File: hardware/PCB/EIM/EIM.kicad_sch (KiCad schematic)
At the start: 37 parts, among them U1 AD9834BRUZ, U2 AD8130ARZ, U3 AD8014ARZ-REEL

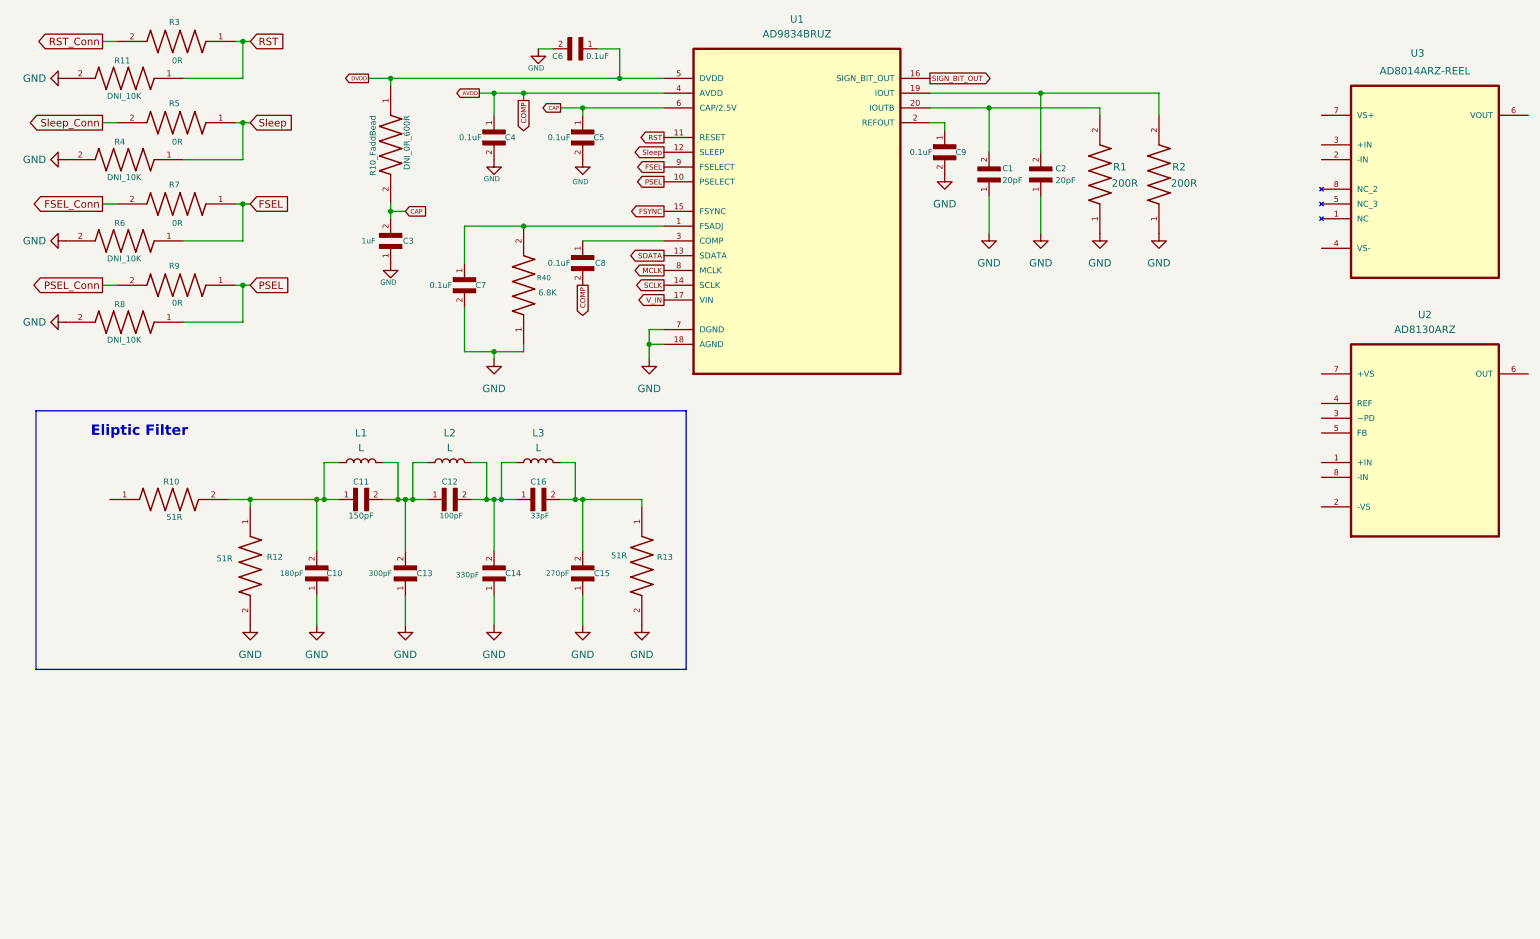
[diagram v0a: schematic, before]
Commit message: MAMS-33 Update schematic for AD9834 and AD8130
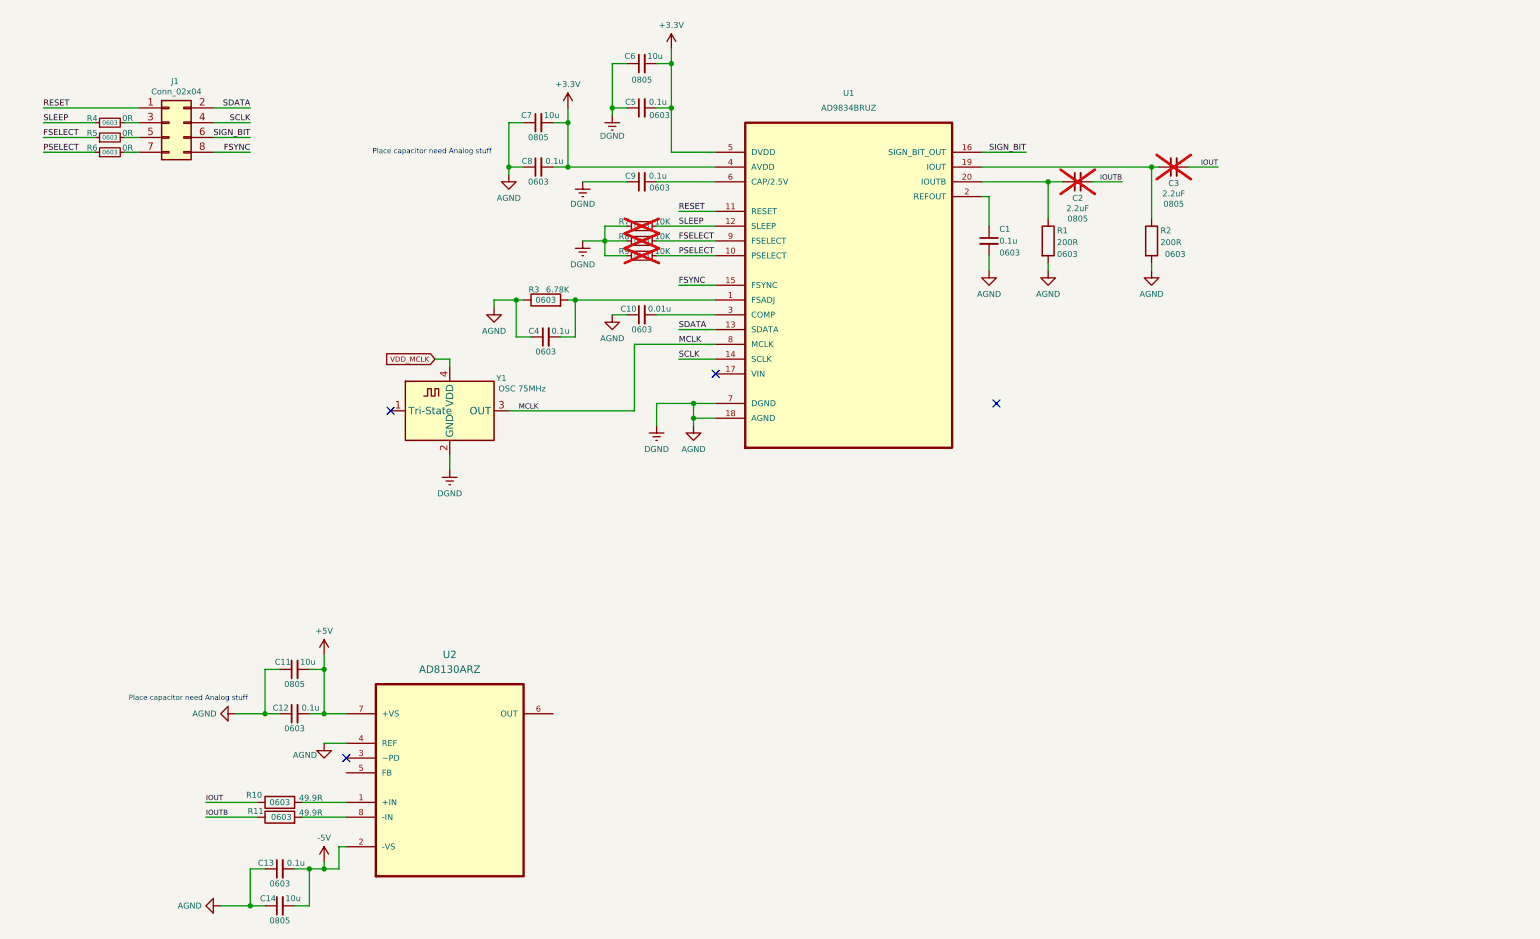
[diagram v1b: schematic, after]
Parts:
- removed C1, C2: 20pF, VJ0603D240KXCAP:CAPC1608X94N, symbol Capacitor_0603:VJ0603D240KXCAP
- removed C10: 180pF, VJ0603D240KXCAP:CAPC1608X94N, symbol Capacitor_0603:VJ0603D240KXCAP
- removed C11: 150pF, VJ0402D3R3DXCAP:CAPC1005X61N, symbol VJ0402D3R3DXCAP:VJ0402D3R3DXCAP
- removed C12: 100pF, VJ0603D240KXCAP:CAPC1608X94N, symbol Capacitor_0603:VJ0603D240KXCAP
- removed C13: 300pF, VJ0603D240KXCAP:CAPC1608X94N, symbol Capacitor_0603:VJ0603D240KXCAP
- removed C14: 330pF, VJ0603D240KXCAP:CAPC1608X94N, symbol Capacitor_0603:VJ0603D240KXCAP
- removed C15: 270pF, VJ0603D240KXCAP:CAPC1608X94N, symbol Capacitor_0603:VJ0603D240KXCAP
- removed C16: 33pF, VJ0603D240KXCAP:CAPC1608X94N, symbol Capacitor_0603:VJ0603D240KXCAP
- removed C3: 1uF, VJ0603D240KXCAP:CAPC1608X94N, symbol Capacitor_0603:VJ0603D240KXCAP
- removed C4, C5, C6, C7, C8, C9: 0.1uF, VJ0402D3R3DXCAP:CAPC1005X61N, symbol VJ0402D3R3DXCAP:VJ0402D3R3DXCAP
- removed L1, L2, L3: L, symbol Device:L
- removed R1, R2: 200R, ERA3AED203V:RES_ERA3AED203V, symbol Resistor_0603:ERA3AED203V
- removed R10, R12, R13: 51R, ERA3AED203V:RES_ERA3AED203V, symbol Resistor_0603:ERA3AED203V
- removed R10_FaddBead: DNI_0R_600R, ERA3AED203V:RES_ERA3AED203V, symbol Resistor_0603:ERA3AED203V
- removed R11, R4, R6, R8: DNI_10K, ERA3AED203V:RES_ERA3AED203V, symbol Resistor_0603:ERA3AED203V
- removed R3, R5, R7, R9: 0R, ERA3AED203V:RES_ERA3AED203V, symbol Resistor_0603:ERA3AED203V
- removed R40: 6.8K, ERA3AED203V:RES_ERA3AED203V, symbol Resistor_0603:ERA3AED203V
- removed U3: AD8014ARZ-REEL, AD8014ARZ-REEL:SOIC127P600X175-8N, symbol AD8014ARZ-REEL:AD8014ARZ-REEL
- added C1, C12, C13, C4, C5, C8, C9: 0.1u, 0603, symbol Device:C_Small
- added C10: 0.01u, 0603, symbol Device:C_Small
- added C11, C14, C6, C7: 10u, 0805, symbol Device:C_Small
- added C2, C3: 2.2uF, 0805, symbol Device:C_Small
- added J1: Conn_02x04, Connector_PinHeader_2.54mm:PinHeader_2x04_P2.54mm_Vertical, symbol Connector_Generic:Conn_02x04_Odd_Even
- added R1, R2: 200R, 0603, symbol Device:R
- added R10, R11: 49.9R, 0603, symbol Device:R
- added R3: 6.78K, 0603, symbol Device:R
- added R4, R5, R6: 0R, 0603, symbol Device:R_Small
- added R7, R8, R9: 10K, 0603, symbol Device:R_Small
- added Y1: OSC 75MHz, Oscillator_SMD_2.5x2.0mm, symbol Oscillator:ECS-2520MV-xxx-xx
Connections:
- net DVDD is gone; now on net +3.3V: U1.5 (DVDD)
- net GND is gone; now on net AGND: U1.18 (AGND), U1.7 (DGND)
- net FSYNC: now also J1.8 (Pin_8)
- net MCLK: now also Y1.3 (OUT)
- net SCLK: now also J1.4 (Pin_4)
- net SDATA: now also J1.2 (Pin_2)
- net at U1.3 (COMP): now also C10.2
- net at U1.1 (FSADJ): now also C4.2, R3.2
- net at U2.1 (+IN): now also R10.2
- net -5V: now reaches U2.2 (-VS)
- net -5V: now also C13.2, C14.2
- net AGND: now reaches U2.4 (REF)
- net AGND: now also C1.2, C10.1, C11.1, C12.1, C13.1, C14.1, C4.1, C5.1, C6.1, C7.1, C8.1, C9.1, R1.2, R2.2, R3.1, R7.1, R8.1, R9.1, Y1.2 (GND)
- net +5V: now reaches U2.7 (+VS)
- net +5V: now also C11.2, C12.2
- net at U2.8 (-IN): now also R11.2
- net at U1.19 (IOUT): now also C3.1, R2.1
- net at U1.2 (REFOUT): now also C1.1
- net at U1.20 (IOUTB): now also C2.1, R1.1
- net AVDD renamed +3.3V
- net +3.3V: now also C5.2, C6.2, C7.2, C8.2
- net CAP: no longer names the net of U1.6 (CAP/2.5V)
- net CAP: now also C9.2
- net FSEL renamed FSELECT
- net FSELECT: now also R5.1, R8.2
- net PSEL renamed PSELECT
- net PSELECT: now also R6.1, R9.2
- net RST renamed RESET
- net RESET: now also J1.1 (Pin_1)
- net SIGN_BIT_OUT renamed SIGN_BIT
- net SIGN_BIT: now also J1.6 (Pin_6)
- net Sleep renamed SLEEP
- net SLEEP: now also R4.1, R7.2
- net V_IN: no longer names the net of U1.17 (VIN)
- new net: J1.7 (Pin_7), R6.2
- new net: J1.5 (Pin_5), R5.2
- new net: J1.3 (Pin_3), R4.2
- new net IOUT: C3.2, R10.1
- new net IOUTB: C2.2, R11.1
- new net VDD_MCLK: Y1.4 (VDD)
- no-connect marks 0 -> 4
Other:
- note added: "Place capacitor need Analog stuff"
- note removed: "Eliptic Filter"
- company: (none) -> University of Science
- title: (none) -> EIM module
- moved on the sheet: U1

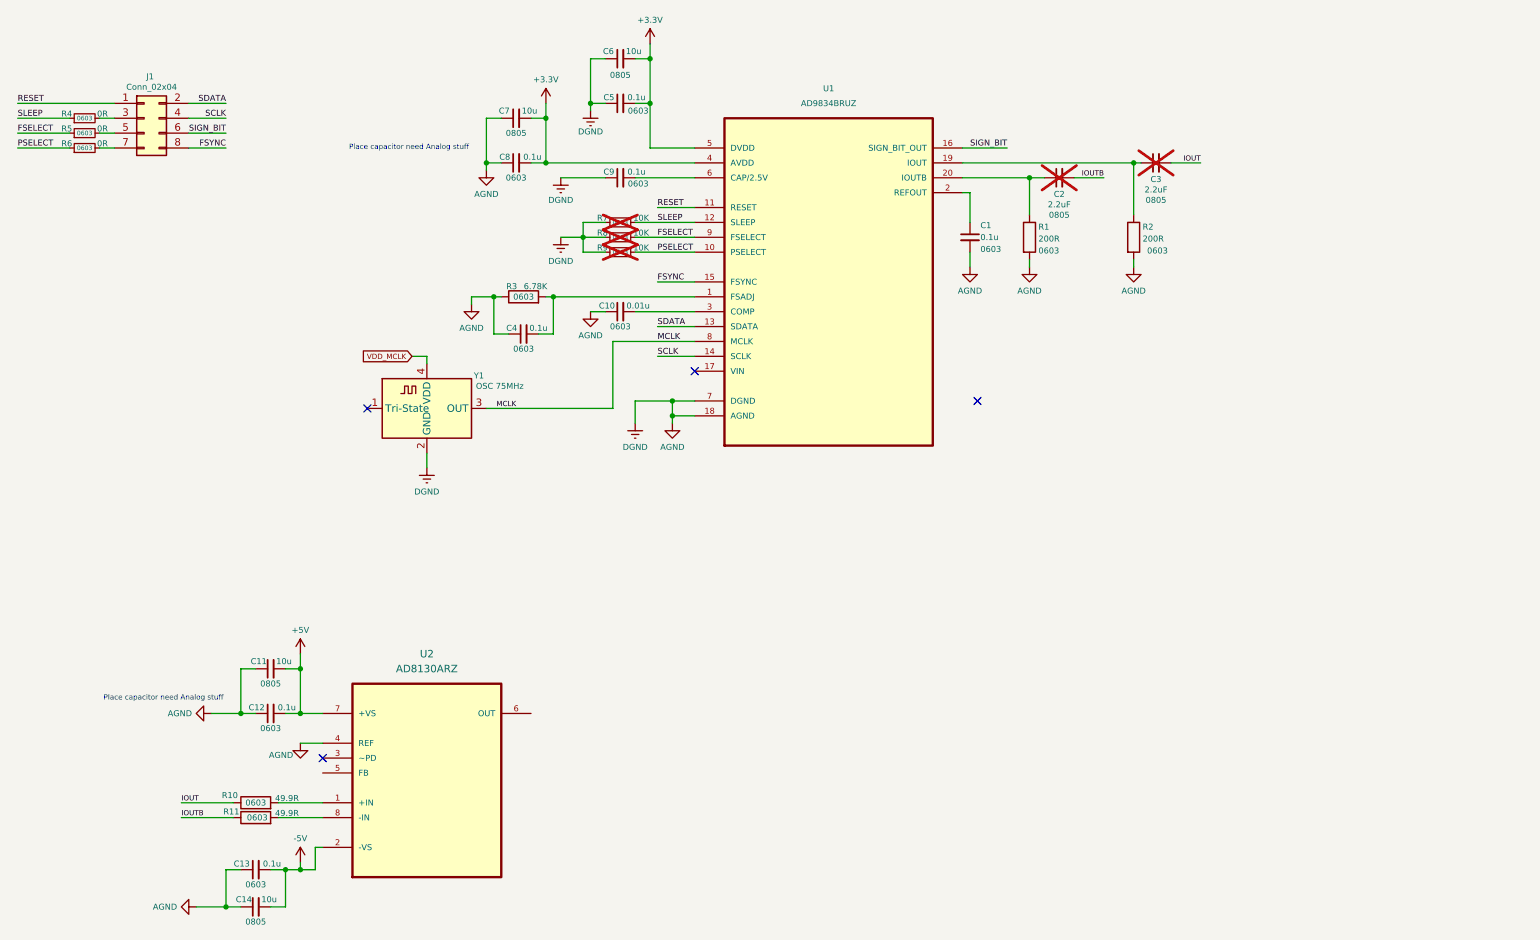
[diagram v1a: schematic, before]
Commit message: MAMS-33 updated schematic for DDS, Diff to Single and Buffer blocks, updated lib for AD8014 used in KiCad
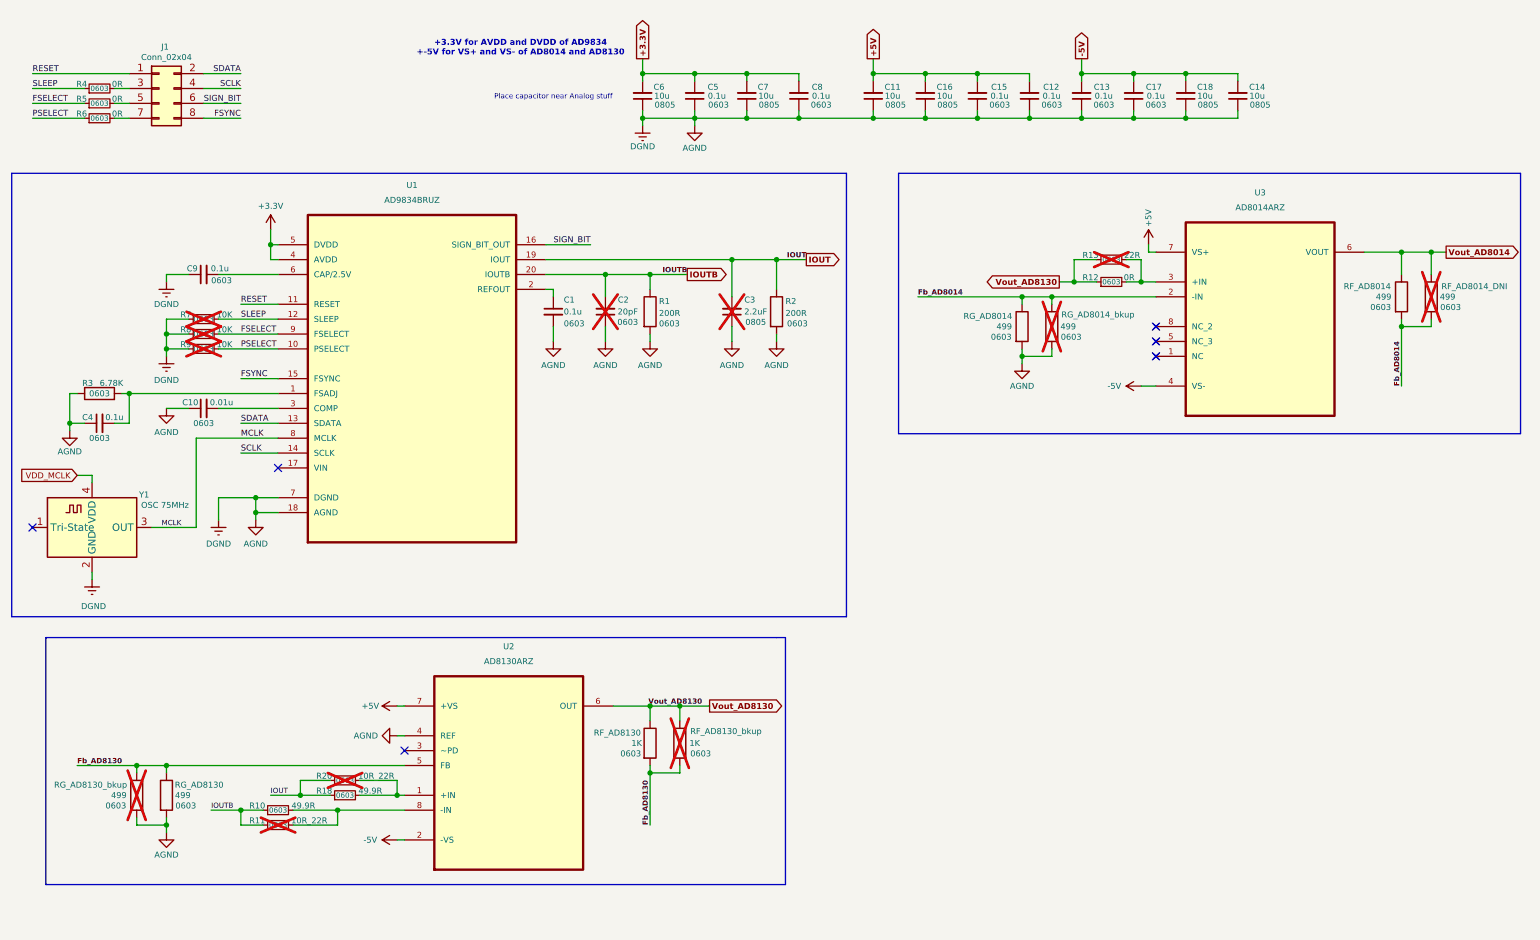
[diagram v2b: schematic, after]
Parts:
- removed R10, R11: 49.9R, 0603, symbol Device:R
- added C15, C17: 0.1u, 0603, symbol Device:C_Small
- added C16, C18: 10u, 0805, symbol Device:C_Small
- added R10, R18: 49.9R, 0603, symbol Device:R_Small
- added R11, R20: 10R_22R, 0603, symbol Device:R_Small
- added R12: 0R, 0603, symbol Device:R_Small
- added R13: 22R, 0603, symbol Device:R_Small
- added RF_AD8014, RF_AD8014_DNI, RG_AD8014, RG_AD8014_bkup, RG_AD8130, RG_AD8130_bkup: 499, 0603, symbol Device:R
- added RF_AD8130, RF_AD8130_bkup: 1K, 0603, symbol Device:R
- added U3: AD8014ARZ, AD8014ARZ:SOIC127P600X175-8N, symbol AD8014ARZ:AD8014ARZ
- C2: value 2.2uF -> 20pF; footprint 0805 -> 0603
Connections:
- net +5V: now also C15.2, C16.2, U3.7 (VS+)
- net -5V: now also C17.2, C18.2, U3.4 (VS-)
- net AGND: now also C2.1, C3.1, C15.1, C16.1, C17.1, C18.1, RG_AD8014.2, RG_AD8014_bkup.2, RG_AD8130.2, RG_AD8130_bkup.2
- net IOUT: now also R2.1, U1.19 (IOUT), R18.1, R20.1
- net IOUTB: now also R1.1, U1.20 (IOUTB), R10.1, R11.1
- net at U2.8 (-IN): now also R10.2, R11.2
- net at U2.1 (+IN): now also R18.2, R20.2
- net Fb_AD8130: now reaches U2.5 (FB)
- net Fb_AD8130: now also RF_AD8130.2, RF_AD8130_bkup.2, RG_AD8130.1, RG_AD8130_bkup.1
- net Vout_AD8130: now reaches U2.6 (OUT)
- net Vout_AD8130: now also R12.1, R13.1, RF_AD8130.1, RF_AD8130_bkup.1
- new net: R12.2, R13.2, U3.3 (+IN)
- new net Fb_AD8014: RF_AD8014.2, RF_AD8014_DNI.2, RG_AD8014.1, RG_AD8014_bkup.1, U3.2 (-IN)
- new net Vout_AD8014: RF_AD8014.1, RF_AD8014_DNI.1, U3.6 (VOUT)
- no-connect marks 4 -> 6
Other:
- note added: "+3.3V for AVDD and DVDD of AD9834 +-5V for VS+ and VS- of AD8014 and AD8130"
- note added: "Place capacitor near Analog stuff"
- note removed: "Place capacitor need Analog stuff"
- moved on the sheet: C1, C10, C11, C12, C13, C14, C2, C3, C4, C5, C6, C7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
